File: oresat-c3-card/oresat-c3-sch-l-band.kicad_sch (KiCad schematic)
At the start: 76 parts, among them U15 Qorvo 856930, U16 AT86RF215, U17 SI4112-GM, U2 BP0805A1308, U23 NCS2-62+, U3 BP0805A1308, U4 BGB741L7ESD, U41 TQP3M9036, U5 BP0805A1308, U7 MAC-24+, X1 TXETALSANF-26.000000

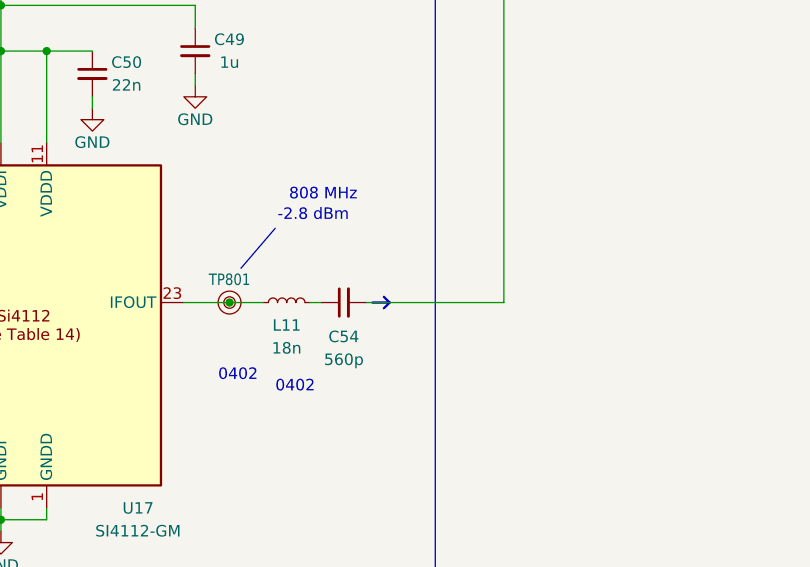
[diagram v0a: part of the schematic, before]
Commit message: Added L band ground cut (Glenn's fault). DRC errrors due to 50 ohm clearance; investigating custom rules now.
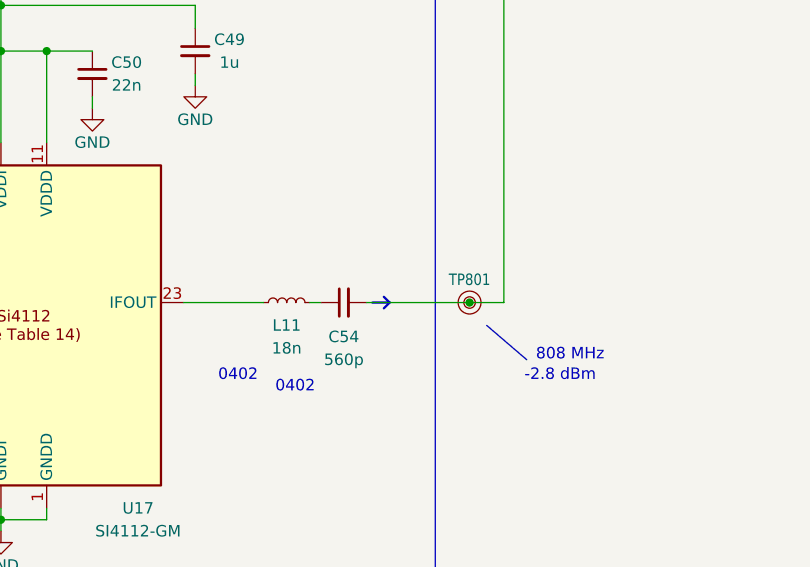
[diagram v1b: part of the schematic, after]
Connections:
- net at L11.1, U17.23 (IFOUT): no longer TP801.1
- net at C54.2, U7.10 (LO): now also TP801.1
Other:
- moved on the sheet: TP801
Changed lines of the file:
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@@
 	(text "-2.8 dBm\n"
 		(exclude_from_sim no)
-		(at 330.454 204.47 0)
+		(at 357.886 222.25 0)
 		(effects
 			(font
@@
 	(text "808 MHz"
 		(exclude_from_sim no)
-		(at 331.724 202.184 0)
+		(at 359.156 219.964 0)
 		(effects
 			(font
@@
 	)
 	(junction
-		(at 325.12 213.36)
-		(diameter 0)
-		(color 0 0 0 0)
-	)
-	(junction
 		(at 299.72 180.34)
 		(diameter 0)
@@
 	)
 	(junction
+		(at 351.79 213.36)
+		(diameter 0)
+		(color 0 0 0 0)
+	)
+	(junction
 		(at 228.6 140.97)
 		(diameter 0)
@@
 	(polyline
 		(pts
-			(xy 330.2 205.105) (xy 326.39 209.55)
+			(xy 353.695 215.9) (xy 358.14 219.71)
 		)
 		(stroke
@@
 	(wire
 		(pts
-			(xy 340.36 213.36) (xy 355.6 213.36)
+			(xy 340.36 213.36) (xy 351.79 213.36)
 		)
 		(stroke
@@
 	(wire
 		(pts
-			(xy 320.04 213.36) (xy 325.12 213.36)
+			(xy 320.04 213.36) (xy 328.93 213.36)
 		)
 		(stroke
@@
 	(wire
 		(pts
-			(xy 325.12 213.36) (xy 328.93 213.36)
-		)
-		(stroke
-			(width 0)
-			(type default)
-		)
-	)
-	(wire
-		(pts
 			(xy 279.4 203.2) (xy 284.48 203.2)
 		)
@@
 	(wire
 		(pts
+			(xy 351.79 213.36) (xy 355.6 213.36)
+		)
+		(stroke
+			(width 0)
+			(type default)
+		)
+	)
+	(wire
+		(pts
 			(xy 137.16 128.27) (xy 139.7 128.27)
 		)
@@
 	(symbol
 		(lib_id "oresat-misc:Test-Point-RF-Probe-Stripline")
-		(at 325.12 213.36 0)
+		(at 351.79 213.36 0)
 		(unit 1)
 		(exclude_from_sim no)
@@
 		(dnp no)
 		(property "Reference" "TP801"
-			(at 325.12 210.82 0)
+			(at 351.79 210.82 0)
 			(effects
 				(font
@@
 		)
 		(property "Value" "~"
-			(at 325.12 205.74 0)
+			(at 351.79 205.74 0)
 			(effects
 				(font
@@
 		)
 		(property "Footprint" "oresat-misc:TestPoint_RF_Probe"
-			(at 325.12 203.2 0)
+			(at 351.79 203.2 0)
 			(effects
 				(font
@@
 		)
 		(property "Datasheet" ""
-			(at 325.12 213.36 0)
+			(at 351.79 213.36 0)
 			(effects
 				(font
@@
 		)
 		(property "Description" "Special test point symbol for RF3B-BC2.0 3 needle RFspring probe"
-			(at 325.12 213.36 0)
+			(at 351.79 213.36 0)
 			(effects
 				(font

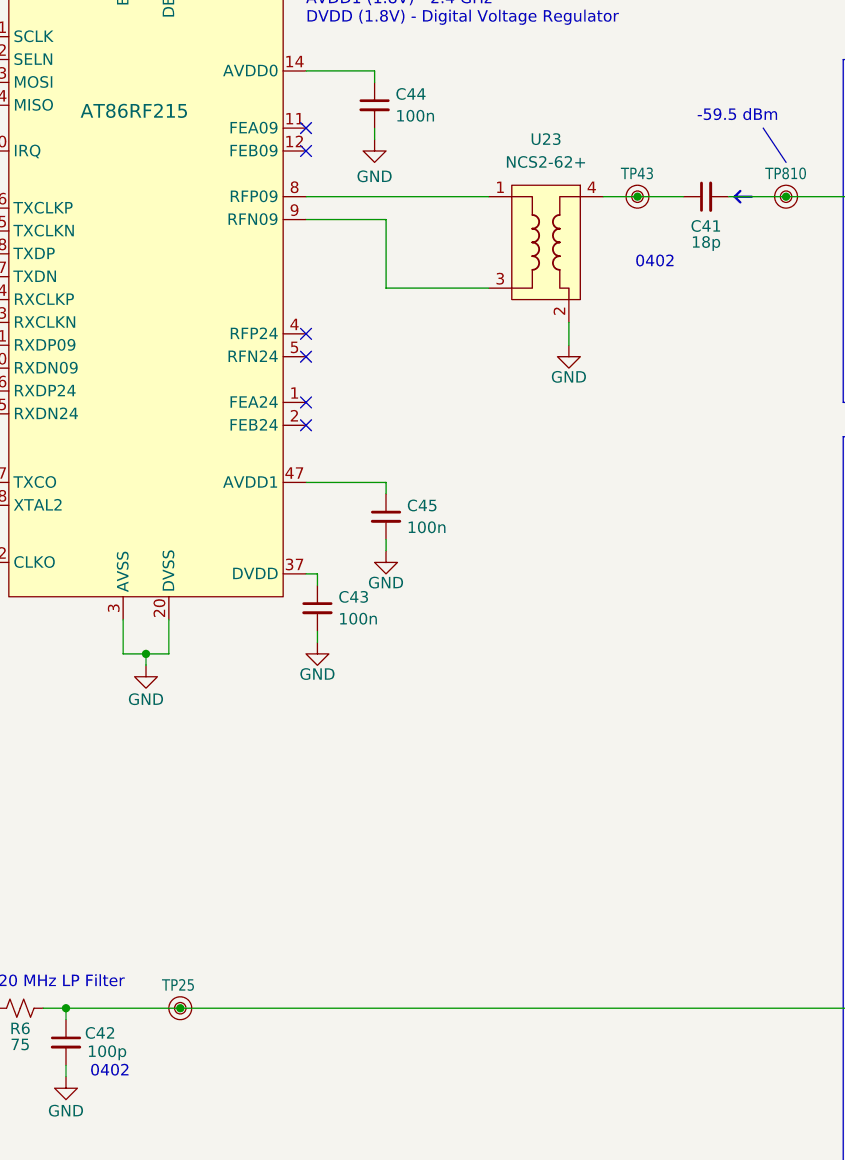
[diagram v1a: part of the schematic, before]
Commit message: Fixed a test point, cleaned up silk screen, and moved date up to today.
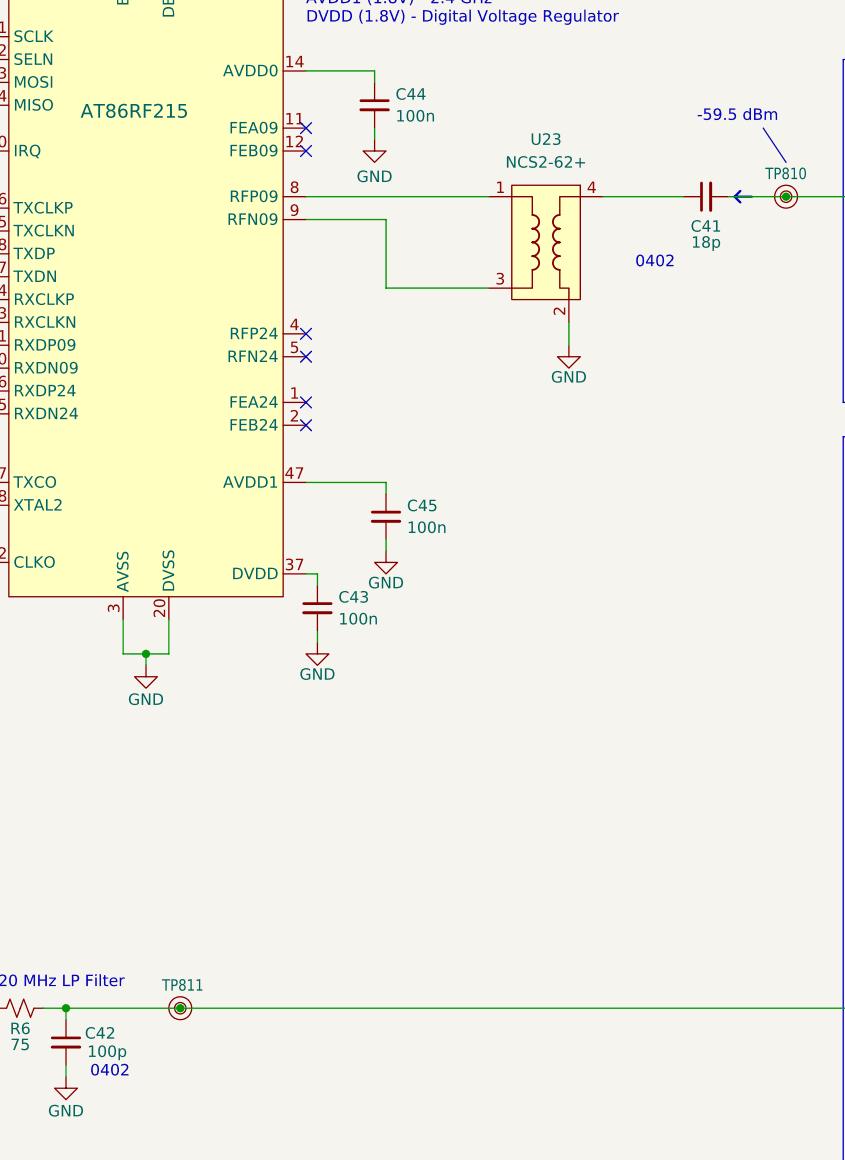
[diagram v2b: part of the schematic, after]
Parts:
- removed TP43: ~, oresat-misc:TestPoint_RF_Probe, symbol oresat-misc:Test-Point-RF-Probe-Stripline
- renumbered TP25 to TP811
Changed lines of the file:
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@@
 	(title_block
 		(title "OreSat C3 Card")
-		(date "2026-03-17")
+		(date "2026-03-20")
 		(rev "7.0")
 		(company "Portland State Aerospace Society")
@@
 	)
 	(junction
-		(at 212.09 140.97)
-		(diameter 0)
-		(color 0 0 0 0)
-	)
-	(junction
 		(at 231.14 60.96)
 		(diameter 0)
@@
 	(wire
 		(pts
-			(xy 212.09 140.97) (xy 217.17 140.97)
-		)
-		(stroke
-			(width 0)
-			(type default)
-		)
-	)
-	(wire
-		(pts
 			(xy 182.88 128.27) (xy 182.88 127)
 		)
@@
 	(wire
 		(pts
-			(xy 208.28 140.97) (xy 212.09 140.97)
+			(xy 208.28 140.97) (xy 217.17 140.97)
 		)
 		(stroke
@@
 	)
 	(symbol
-		(lib_id "oresat-misc:Test-Point-RF-Probe-Stripline")
-		(at 212.09 140.97 180)
-		(unit 1)
-		(exclude_from_sim no)
-		(in_bom no)
-		(on_board yes)
-		(dnp no)
-		(property "Reference" "TP43"
-			(at 212.09 138.43 0)
-			(effects
-				(font
-					(size 1.27 1.0795)
-				)
-			)
-		)
-		(property "Value" "~"
-			(at 212.09 148.59 0)
-			(effects
-				(font
-					(size 1.27 1.27)
-				)
-				(hide yes)
-			)
-		)
-		(property "Footprint" "oresat-misc:TestPoint_RF_Probe"
-			(at 212.09 151.13 0)
-			(effects
-				(font
-					(size 1.27 1.27)
-				)
-				(hide yes)
-			)
-		)
-		(property "Datasheet" ""
-			(at 212.09 140.97 0)
-			(effects
-				(font
-					(size 1.27 1.27)
-				)
-				(hide yes)
-			)
-		)
-		(property "Description" "Special test point symbol for RF3B-BC2.0 3 needle RFspring probe"
-			(at 212.09 140.97 0)
-			(effects
-				(font
-					(size 1.27 1.27)
-				)
-				(hide yes)
-			)
-		)
-		(pin "1"
-		)
-		(instances
-			(project "oresat-c3"
-				(path "/65d12cdd-c326-4033-9053-c59fa4e0b25e/1b68ea4b-cacf-4529-b1d4-9be5d7c1043c"
-					(reference "TP43")
-					(unit 1)
-				)
-			)
-		)
-	)
-	(symbol
 		(lib_id "Device:RFShield_TwoPieces")
 		(at 46.99 207.01 0)
@@
 		(on_board yes)
 		(dnp no)
-		(property "Reference" "TP25"
+		(property "Reference" "TP811"
 			(at 159.258 228.6 90)
 			(effects
@@
 			(project "oresat-c3"
 				(path "/65d12cdd-c326-4033-9053-c59fa4e0b25e/1b68ea4b-cacf-4529-b1d4-9be5d7c1043c"
-					(reference "TP25")
+					(reference "TP811")
 					(unit 1)
 				)

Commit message: Changed WDT tantalums to space-rated tantalums (fun) and fixed some BOM issues. Also possibly more silk screen cleanup.
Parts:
- C12, C143, C144, C145, C37, C38, C4, C41, C42, C50, C51, C54: DST Digi-Key -> DigiKey
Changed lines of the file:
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@@
 			)
 		)
-		(property "DST" "Digi-Key"
+		(property "DST" "DigiKey"
 			(at 309.88 187.96 0)
 			(effects
@@
 			)
 		)
-		(property "DST" "Digi-Key"
+		(property "DST" "DigiKey"
 			(at 219.71 140.97 0)
 			(effects
@@
 			)
 		)
-		(property "DST" "Digi-Key"
+		(property "DST" "DigiKey"
 			(at 292.1 187.96 0)
 			(effects
@@
 			)
 		)
-		(property "DST" "Digi-Key"
+		(property "DST" "DigiKey"
 			(at 314.96 60.96 0)
 			(effects
@@
 			)
 		)
-		(property "DST" "Digi-Key"
+		(property "DST" "DigiKey"
 			(at 148.59 234.95 0)
 			(effects
@@
 			)
 		)
-		(property "DST" "Digi-Key"
+		(property "DST" "DigiKey"
 			(at 242.57 146.05 0)
 			(effects
@@
 			)
 		)
-		(property "DST" "Digi-Key"
+		(property "DST" "DigiKey"
 			(at 262.89 146.05 0)
 			(effects
@@
 			)
 		)
-		(property "DST" "Digi-Key"
+		(property "DST" "DigiKey"
 			(at 173.99 41.91 0)
 			(effects
@@
 			)
 		)
-		(property "DST" "Digi-Key"
+		(property "DST" "DigiKey"
 			(at 285.75 60.96 0)
 			(effects
@@
 			)
 		)
-		(property "DST" "Digi-Key"
+		(property "DST" "DigiKey"
 			(at 337.82 213.36 0)
 			(effects
@@
 			)
 		)
-		(property "DST" "Digi-Key"
+		(property "DST" "DigiKey"
 			(at 283.21 48.26 0)
 			(effects
@@
 			)
 		)
-		(property "DST" "Digi-Key"
+		(property "DST" "DigiKey"
 			(at 252.73 146.05 0)
 			(effects

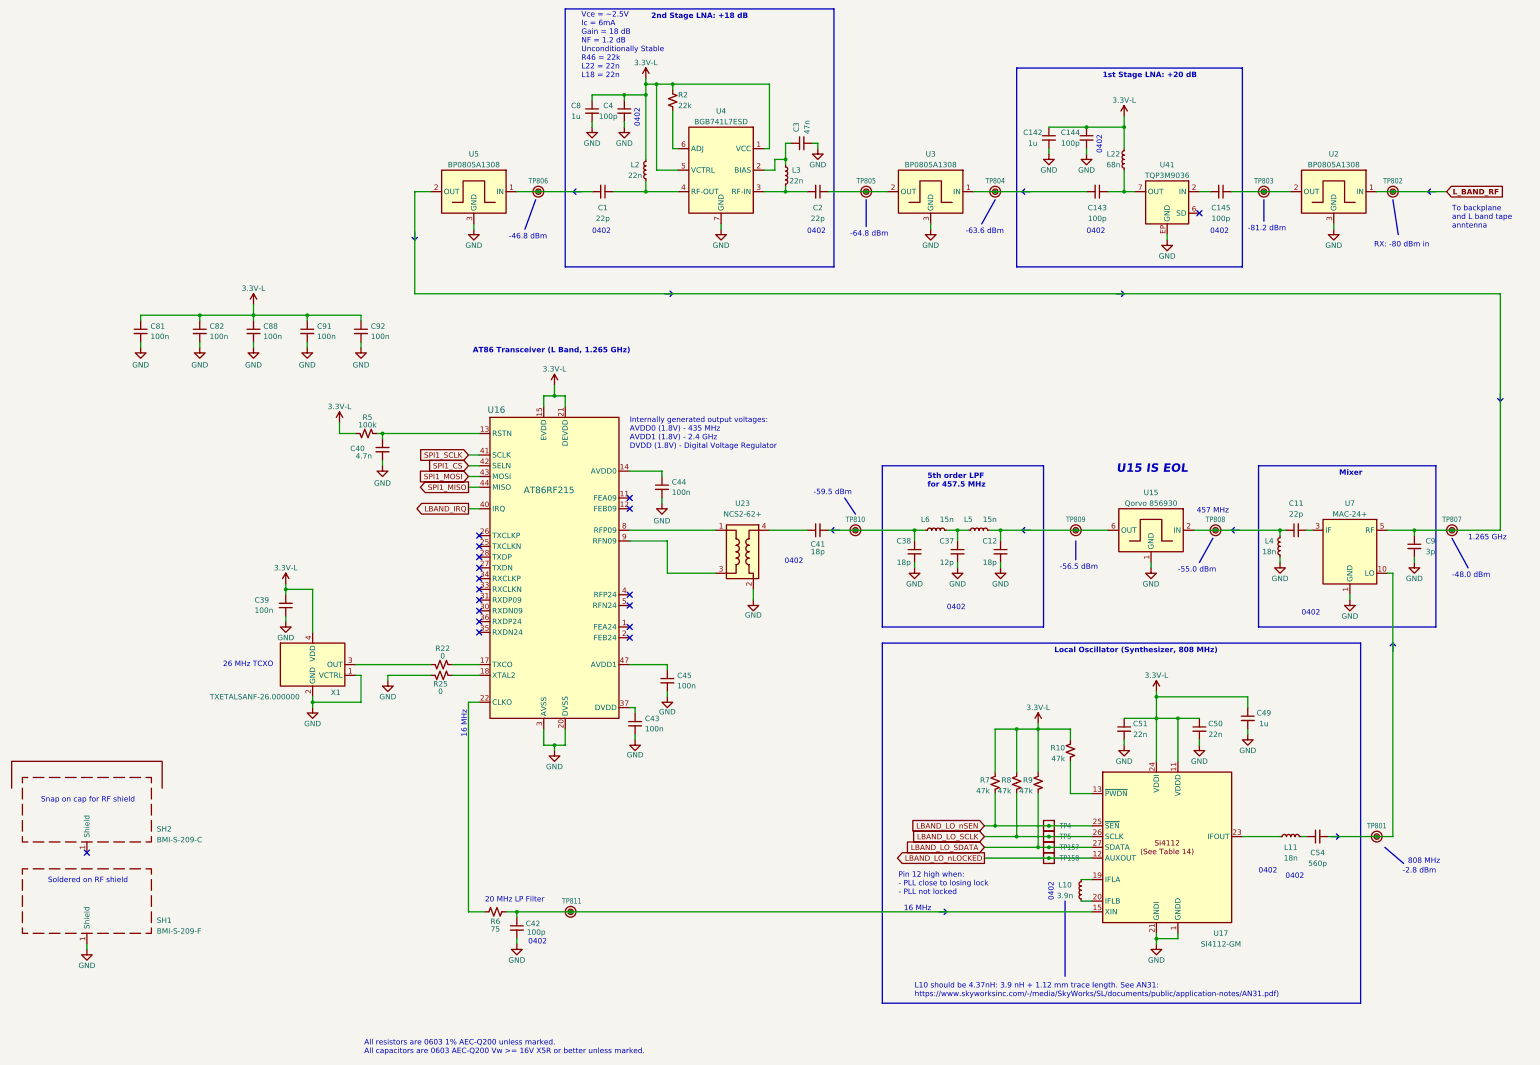
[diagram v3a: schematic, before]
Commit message: Removed unecessary L band 5th order filter. Moved UHF to 401/436 variants
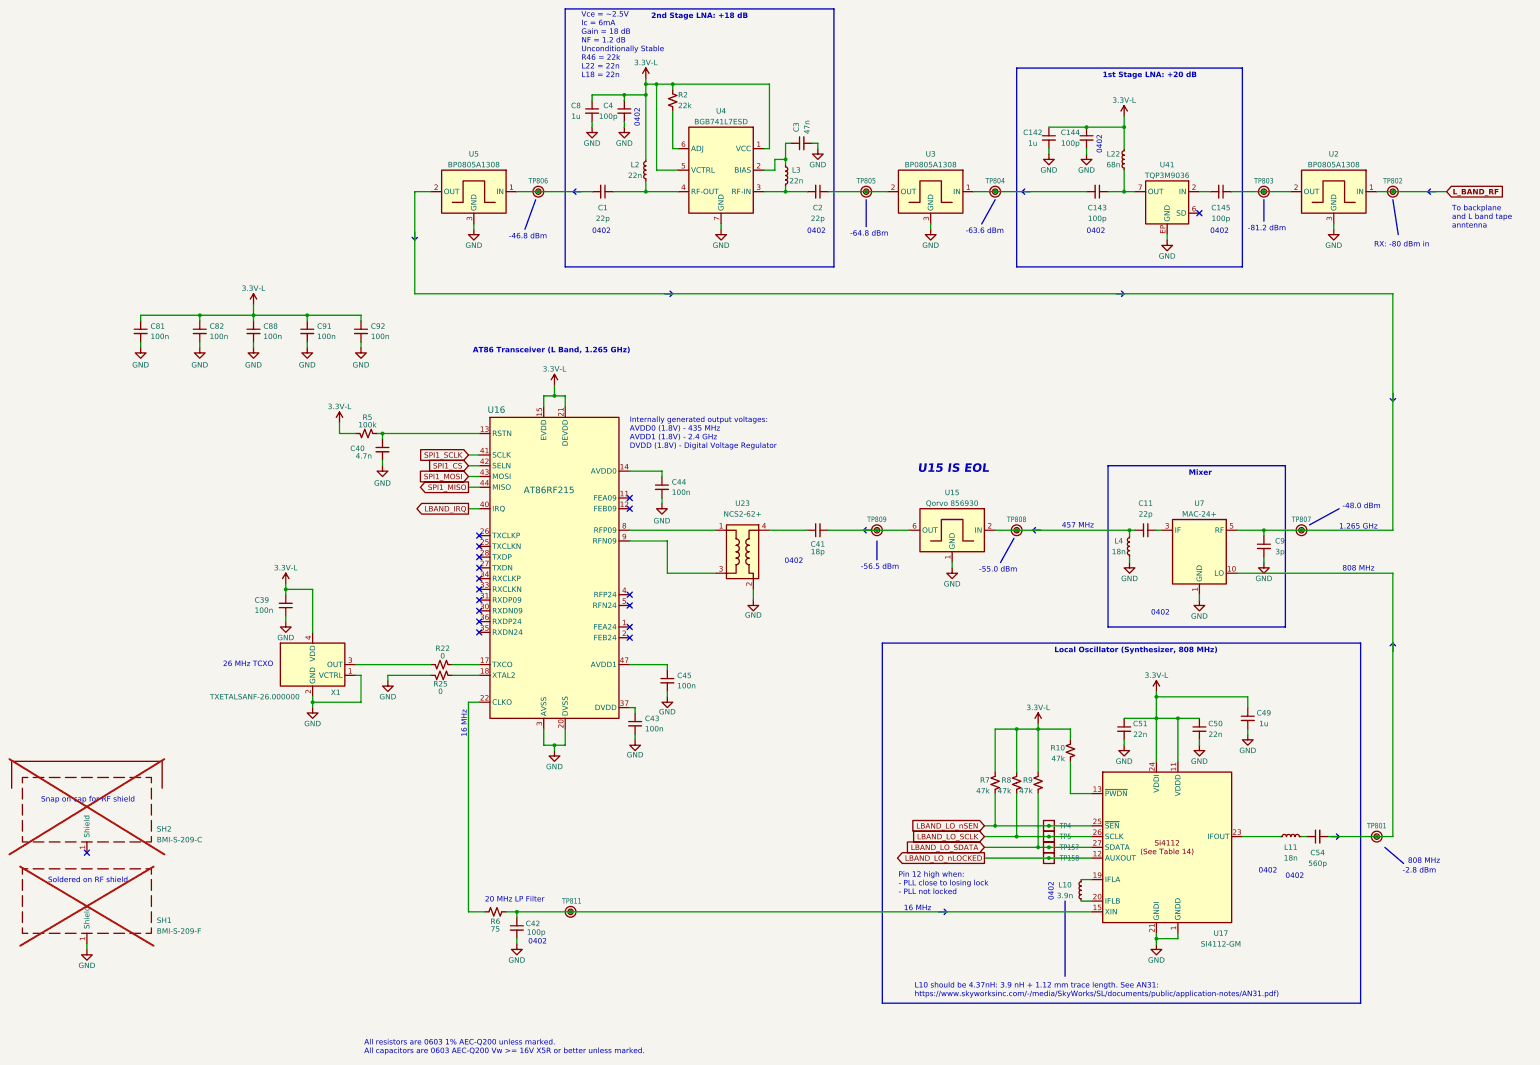
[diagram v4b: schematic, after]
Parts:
- removed C12, C38: 18p, oresat-passives:0402-B-NOSILK, symbol Device:C_Small
- removed C37: 12p, oresat-passives:0402-B-NOSILK, symbol Device:C_Small
- removed L5, L6: 15n, Inductor_SMD:L_0402_1005Metric, symbol Device:L_Small
- removed TP810: ~, oresat-misc:TestPoint_RF_Probe, symbol oresat-misc:Test-Point-RF-Probe-Stripline
- SH1, SH2: now not fitted
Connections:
- net at C41.2: now also TP809.1, U15.6 (OUT)
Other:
- note removed: "-59.5 dBm"
- note removed: "5th order LPF for 457.5 MHz"
- moved on the sheet: C11, C9, L4, TP807, TP808, TP809, U15, U7
